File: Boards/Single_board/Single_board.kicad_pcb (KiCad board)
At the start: 2 copper layers, 169.9 x 190.9 mm, 132 parts, among them J1 AUX_I2C_1, J2 AUX_I2C_2, J3 USB_C_Receptacle_USB2.0_16P, J4 ICSP, Q1 SI2306, Q10 SI2306, Q11 SI2306, Q12 SI2306, Q13 SI2306, Q14 SI2306, Q15 SI2306, Q2 SI2306, Q3 SI2306, Q4 SI2306, Q5 SI2306, Q6 SI2306, Q7 SI2306, Q8 SI2306, Q9 SI2306, SW1 +, SW10 5, SW11 2, SW12 9, SW13 PRO, SW14 6, SW15 3, SW16 CLR, SW17 ENTR, SW18 RSET, SW19 KEYREL, SW2 VERB, SW3 NOUN, SW4 0, SW5 7, SW6 -, SW7 4, SW8 1, SW9 8, U1 PCF8575, U2 ATmega328P-A, U3 CH340C

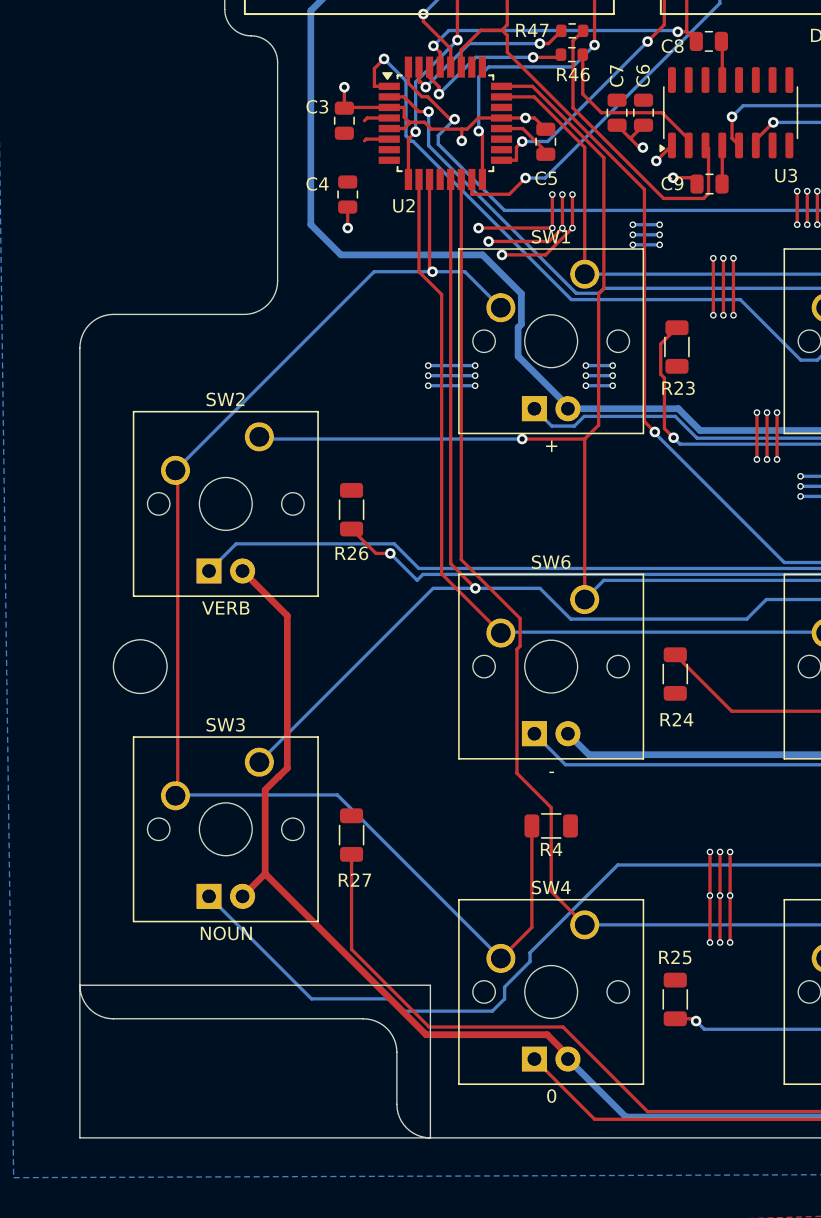
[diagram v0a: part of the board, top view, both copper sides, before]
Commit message: Connect AVCC to VCC
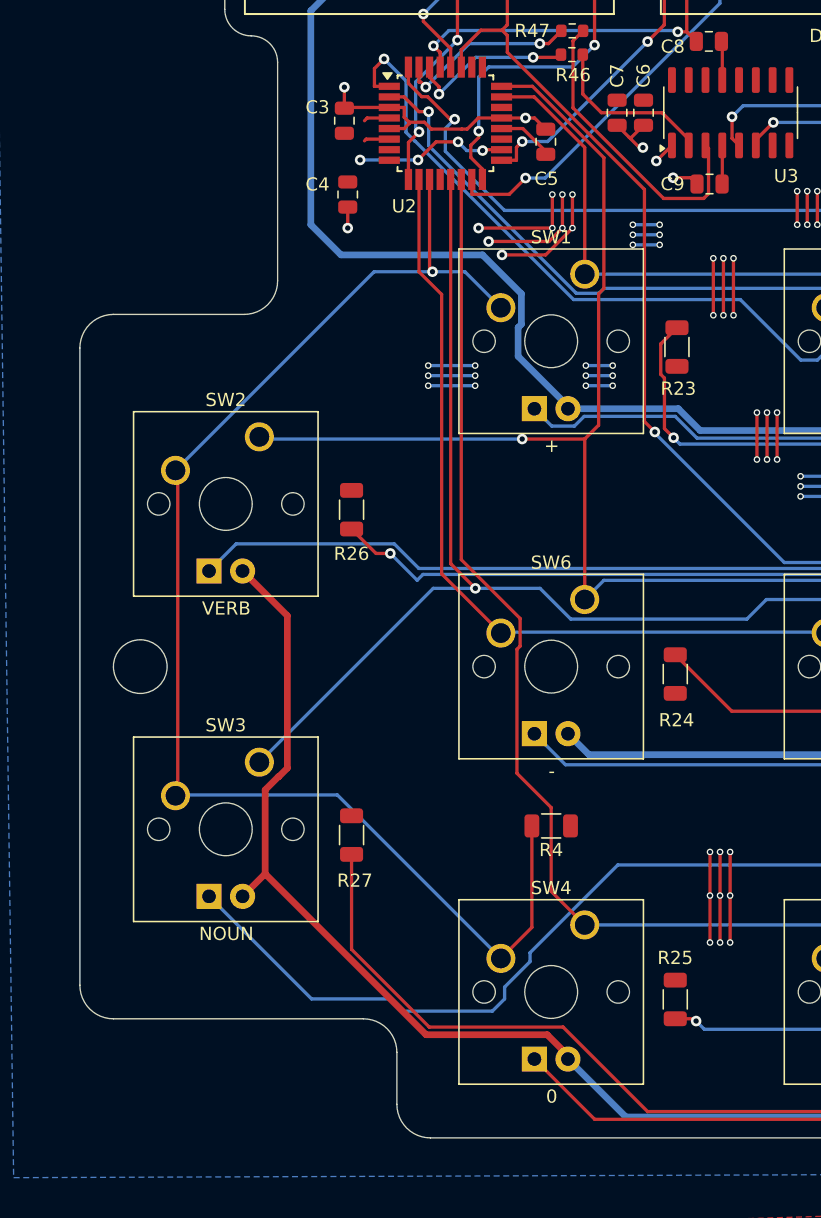
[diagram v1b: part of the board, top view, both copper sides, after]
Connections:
- U2 pad 18: unconnected-(U2-AVCC-Pad18) -> +5V
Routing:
- net +5V: track 130.0 -> 141.6 mm, vias 78 -> 82
- net GND: track 278.3 -> 277.4 mm, vias 116 -> 115
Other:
- outline, holes or cut-outs redrawn

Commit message: Better via placement
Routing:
- net X4: track 221.1 -> 220.4 mm

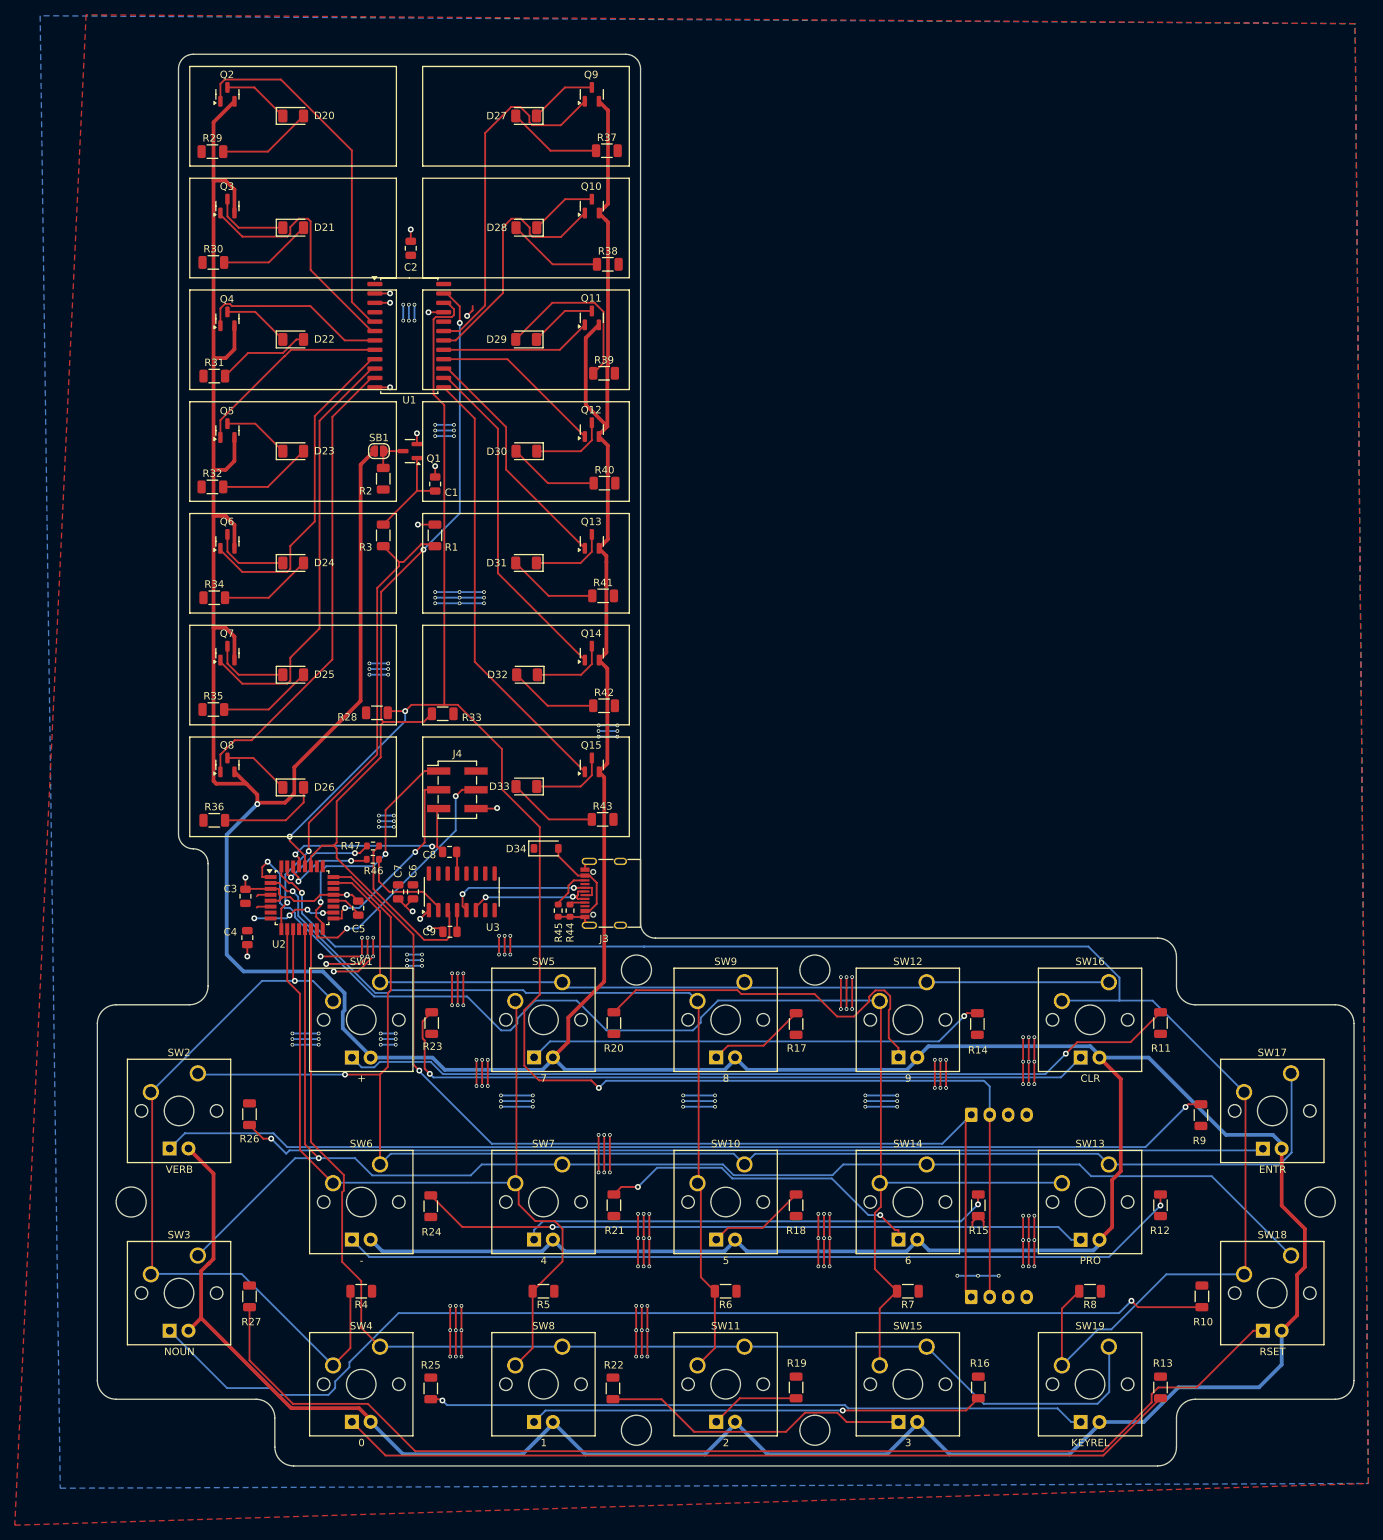
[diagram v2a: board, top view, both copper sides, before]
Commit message: Start RGB LED + hotswap socket redesign of single board
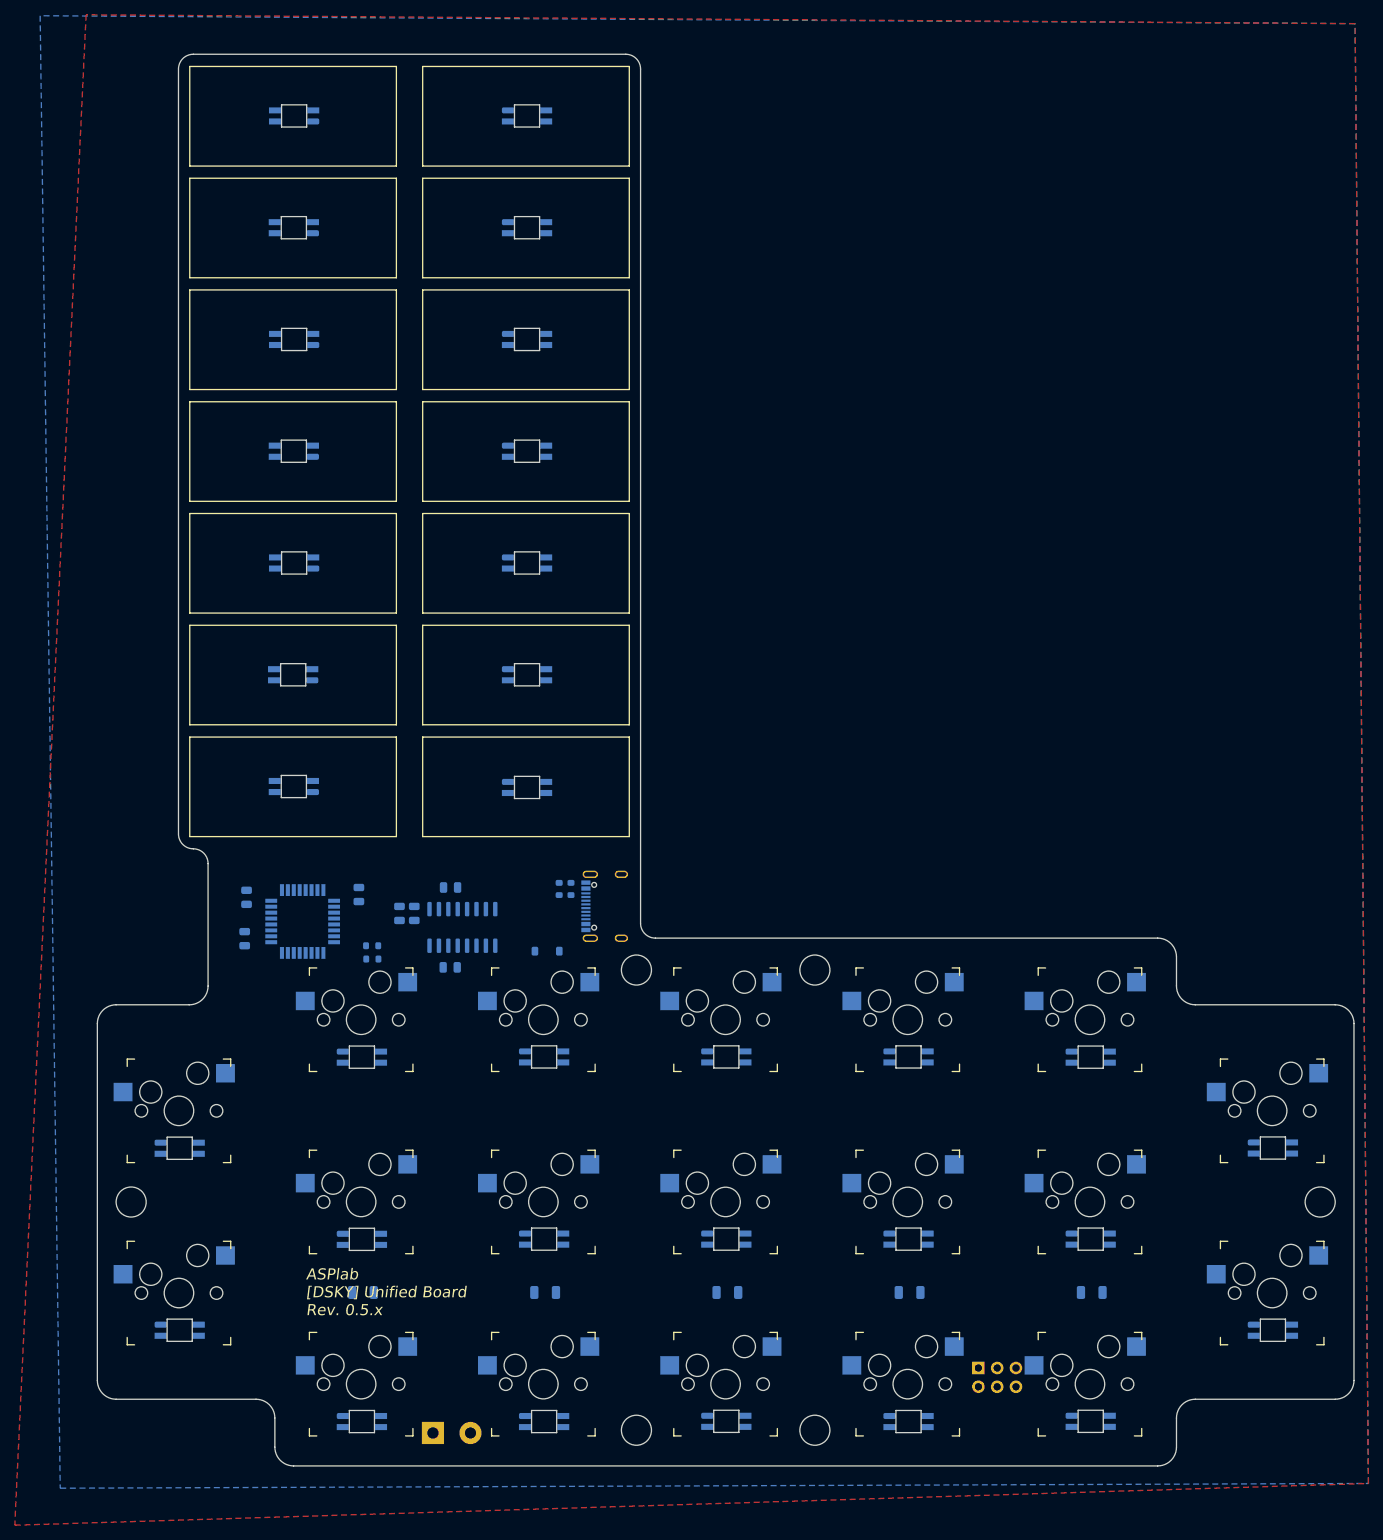
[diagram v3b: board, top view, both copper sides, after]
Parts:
- removed C1: 1nF, Capacitor_SMD:C_0805_2012Metric
- removed C2: 1uF, Capacitor_SMD:C_0805_2012Metric
- removed J4: ICSP, Connector_PinHeader_2.54mm:PinHeader_2x03_P2.54mm_Vertical_SMD
- removed Q1, Q10, Q11, Q12, Q13, Q14, Q15, Q2, Q3, Q4, Q5, Q6, Q7, Q8, Q9: SI2306, Package_TO_SOT_SMD:SOT-23
- removed R1, R28, R33: 10k, Resistor_SMD:R_1206_3216Metric
- removed R10, R11, R12, R13, R14, R15, R16, R17, R18, R19, R20, R21, R22, R23, R24, R25, R26, R27, R9: 1K, Resistor_SMD:R_1206_3216Metric
- removed R2, R29, R3, R30, R31, R32, R34: 1k, Resistor_SMD:R_1206_3216Metric
- removed R35, R36, R37, R38, R39, R40, R41, R42, R43: 220, Resistor_SMD:R_1206_3216Metric
- removed SB1: 0, Jumper:SolderJumper-2_P1.3mm_Open_RoundedPad1.0x1.5mm
- removed U1: PCF8575, Package_SO:SOIC-24W_7.5x15.4mm_P1.27mm
- C3, C4, C5, C6, C7, C8, C9, D34, J3, R4, R44, R45, R46, R47, R5, R6, R7, R8, U2, U3: moved to B.Cu
- D1, D10, D11, D12, D13, D14, D15, D16, D17, D18, D19, D2, D3, D4, D5, D6, D7, D8, D9: value White LED -> SK6812MINI; footprint Switch_Misc:MX-LED-PolarityMarked -> Project Libraries:SK6812-MINI-E; moved to B.Cu
- D20, D21, D22, D23, D24: value White LED -> SK6812MINI; footprint LED_SMD:LED_1206_3216Metric -> Project Libraries:SK6812-MINI-E; moved to B.Cu
- D25, D26, D27, D28, D29, D30, D31, D32, D33: value Orange LED -> SK6812MINI; footprint LED_SMD:LED_1206_3216Metric -> Project Libraries:SK6812-MINI-E; moved to B.Cu
- J1: value AUX_I2C_1 -> POWER; footprint Connector_JST:JST_XH_B4B-XH-A_1x04_P2.50mm_Vertical -> TerminalBlock:TerminalBlock_bornier-2_P5.08mm
- J2: value AUX_I2C_2 -> ICSP; footprint Connector_JST:JST_XH_B4B-XH-A_1x04_P2.50mm_Vertical -> Connector_PinHeader_2.54mm:PinHeader_2x03_P2.54mm_Horizontal
- SW1, SW10, SW11, SW12, SW13, SW14, SW15, SW16, SW17, SW18, SW19, SW2, SW3, SW4, SW5, SW6, SW7, SW8, SW9: footprint Switch_Misc:SW_Cherry_MX_1.00u_PCB -> Project Libraries:Kailh_socket_MX
- moved D1 148.0 mm to (281.7, 183.6), turned to 180 degrees
- moved D2 148.0 mm to (281.7, 208.3), turned to 180 degrees
- moved D18 147.8 mm to (133.9, 183.7), turned to 180 degrees
- moved D19 147.8 mm to (133.9, 208.3), turned to 180 degrees
- moved D3 98.8 mm to (257.0, 171.4), turned to 180 degrees
- moved D4 98.8 mm to (257.0, 196.0), turned to 180 degrees
- moved D5 98.8 mm to (257.0, 220.6), turned to 180 degrees
- moved D15 98.6 mm to (158.5, 171.4), turned to 180 degrees
- moved D16 98.6 mm to (158.5, 196.0), turned to 180 degrees
- moved D17 98.6 mm to (158.5, 220.6), turned to 180 degrees
- moved J1 75.1 mm to (168.1, 222.2)
- moved D6 49.6 mm to (232.4, 171.3), turned to 180 degrees
- moved D7 49.6 mm to (232.4, 196.0), turned to 180 degrees
- moved D8 49.6 mm to (232.4, 220.6), turned to 180 degrees
- moved D12 49.4 mm to (183.1, 171.3), turned to 180 degrees
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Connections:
- D1 pad 1: PWMCom -> Net-(D1-DOUT)
- D1 pad 2: Net-(D1-A) -> unconnected-(D1-VSS-Pad2)
- D10 pad 1: PWMCom -> Net-(D10-DOUT)
- D10 pad 2: Net-(D10-A) -> unconnected-(D10-VSS-Pad2)
- D11 pad 1: PWMCom -> Net-(D11-DOUT)
- D11 pad 2: Net-(D11-A) -> GND
- D12 pad 1: PWMCom -> Net-(D12-DOUT)
- D12 pad 2: Net-(D12-A) -> GND
- D13 pad 1: PWMCom -> Net-(D13-DOUT)
- D13 pad 2: Net-(D13-A) -> GND
- D14 pad 1: PWMCom -> Net-(D14-DOUT)
- D14 pad 2: Net-(D14-A) -> GND
- D15 pad 1: PWMCom -> Net-(D15-DOUT)
- D15 pad 2: Net-(D15-A) -> GND
- D16 pad 1: PWMCom -> Net-(D16-DOUT)
- D16 pad 2: Net-(D16-A) -> GND
- D17 pad 1: PWMCom -> Net-(D17-DOUT)
- D17 pad 2: Net-(D17-A) -> GND
- D18 pad 1: PWMCom -> Net-(D18-DOUT)
- D18 pad 2: Net-(D18-A) -> GND
- D19 pad 1: PWMCom -> Net-(D19-DOUT)
- D19 pad 2: Net-(D19-A) -> GND
- D2 pad 1: PWMCom -> Net-(D2-DOUT)
- D2 pad 2: Net-(D2-A) -> unconnected-(D2-VSS-Pad2)
- D20 pad 1: Net-(D20-K) -> Net-(D20-DOUT)
- D20 pad 2: Net-(D20-A) -> unconnected-(D20-VSS-Pad2)
- D21 pad 1: Net-(D21-K) -> Net-(D21-DOUT)
- D21 pad 2: Net-(D21-A) -> GND
- D22 pad 1: Net-(D22-K) -> Net-(D22-DOUT)
- D22 pad 2: Net-(D22-A) -> unconnected-(D22-VSS-Pad2)
- D23 pad 1: Net-(D23-K) -> Net-(D23-DOUT)
- D23 pad 2: Net-(D23-A) -> GND
- D24 pad 1: Net-(D24-K) -> Net-(D24-DOUT)
- D24 pad 2: Net-(D24-A) -> unconnected-(D24-VSS-Pad2)
- D25 pad 1: Net-(D25-K) -> Net-(D25-DOUT)
- D25 pad 2: Net-(D25-A) -> GND
- D26 pad 1: Net-(D26-K) -> Net-(D26-DOUT)
- D26 pad 2: Net-(D26-A) -> unconnected-(D26-VSS-Pad2)
- D27 pad 1: Net-(D27-K) -> Net-(D27-DOUT)
- D27 pad 2: Net-(D27-A) -> GND
- D28 pad 1: Net-(D28-K) -> Net-(D28-DOUT)
- D28 pad 2: Net-(D28-A) -> unconnected-(D28-VSS-Pad2)
- D29 pad 1: Net-(D29-K) -> Net-(D29-DOUT)
- D29 pad 2: Net-(D29-A) -> GND
- D3 pad 1: PWMCom -> Net-(D3-DOUT)
- D3 pad 2: Net-(D3-A) -> unconnected-(D3-VSS-Pad2)
- D30 pad 1: Net-(D30-K) -> Net-(D30-DOUT)
- D30 pad 2: Net-(D30-A) -> unconnected-(D30-VSS-Pad2)
- D31 pad 1: Net-(D31-K) -> Net-(D31-DOUT)
- D31 pad 2: Net-(D31-A) -> GND
- D32 pad 1: Net-(D32-K) -> Net-(D21-DIN)
- D32 pad 2: Net-(D32-A) -> unconnected-(D32-VSS-Pad2)
- D33 pad 1: Net-(D33-K) -> unconnected-(D33-DOUT-Pad1)
- D33 pad 2: Net-(D33-A) -> GND
- D4 pad 1: PWMCom -> Net-(D4-DOUT)
- D4 pad 2: Net-(D4-A) -> unconnected-(D4-VSS-Pad2)
- D5 pad 1: PWMCom -> Net-(D5-DOUT)
- D5 pad 2: Net-(D5-A) -> unconnected-(D5-VSS-Pad2)
- D6 pad 1: PWMCom -> Net-(D6-DOUT)
- D6 pad 2: Net-(D6-A) -> unconnected-(D6-VSS-Pad2)
- D7 pad 1: PWMCom -> Net-(D7-DOUT)
- D7 pad 2: Net-(D7-A) -> unconnected-(D7-VSS-Pad2)
- D8 pad 1: PWMCom -> Net-(D8-DOUT)
- D8 pad 2: Net-(D8-A) -> unconnected-(D8-VSS-Pad2)
- D9 pad 1: PWMCom -> Net-(D10-DIN)
- D9 pad 2: Net-(D9-A) -> unconnected-(D9-VSS-Pad2)
- J1 pad 1: SDA -> GND
- J1 pad 2: SCL -> +5V
- J2 pad 1: SDA -> MISO
- J2 pad 2: SCL -> +5V
- J2 pad 3: +5V -> SCK
- J2 pad 4: GND -> MOSI
- U2 pad 27: SDA -> unconnected-(U2-PC4-Pad27)
- U2 pad 28: SCL -> unconnected-(U2-PC5-Pad28)
- U2 pad 9: PWM -> RGB_DIN
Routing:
- net PWMCom: track 890.2 -> 0.00 mm, vias 1 -> 0
- net GND: track 277.4 -> 0.00 mm, vias 115 -> 0
- net SCL: track 244.1 -> 0.00 mm, vias 3 -> 0
- net SDA: track 236.0 -> 0.00 mm, vias 3 -> 0
- net X4: track 220.4 -> 0.00 mm, vias 1 -> 0
- net Y1: track 205.8 -> 0.00 mm, vias 1 -> 0
- net Y2: track 192.9 -> 0.00 mm, vias 1 -> 0
- net X3: track 180.9 -> 0.00 mm, vias 1 -> 0
- net Y3: track 169.1 -> 0.00 mm
- net Net-(D19-A): track 156.7 -> 0.00 mm
- net Net-(D2-A): track 149.7 -> 0.00 mm, vias 1 -> 0
- net Net-(D1-A): track 143.5 -> 0.00 mm, vias 1 -> 0
- net +5V: track 141.4 -> 0.00 mm, vias 82 -> 0
- net Net-(D18-A): track 138.9 -> 0.00 mm, vias 1 -> 0
- net X1: track 117.8 -> 0.00 mm
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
